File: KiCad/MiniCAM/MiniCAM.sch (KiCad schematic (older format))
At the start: 69 parts, among them J1 SMA-J-P-H-RA-TH1, J2 Conn_01x02, J3 Conn_01x03, J4 Conn_02x03_Odd_Even, U1 NCV8154MW180280TBG, U2 DS90UB933-Q1, U3 MT9P031, U4 SiT_2.5mmx2mm

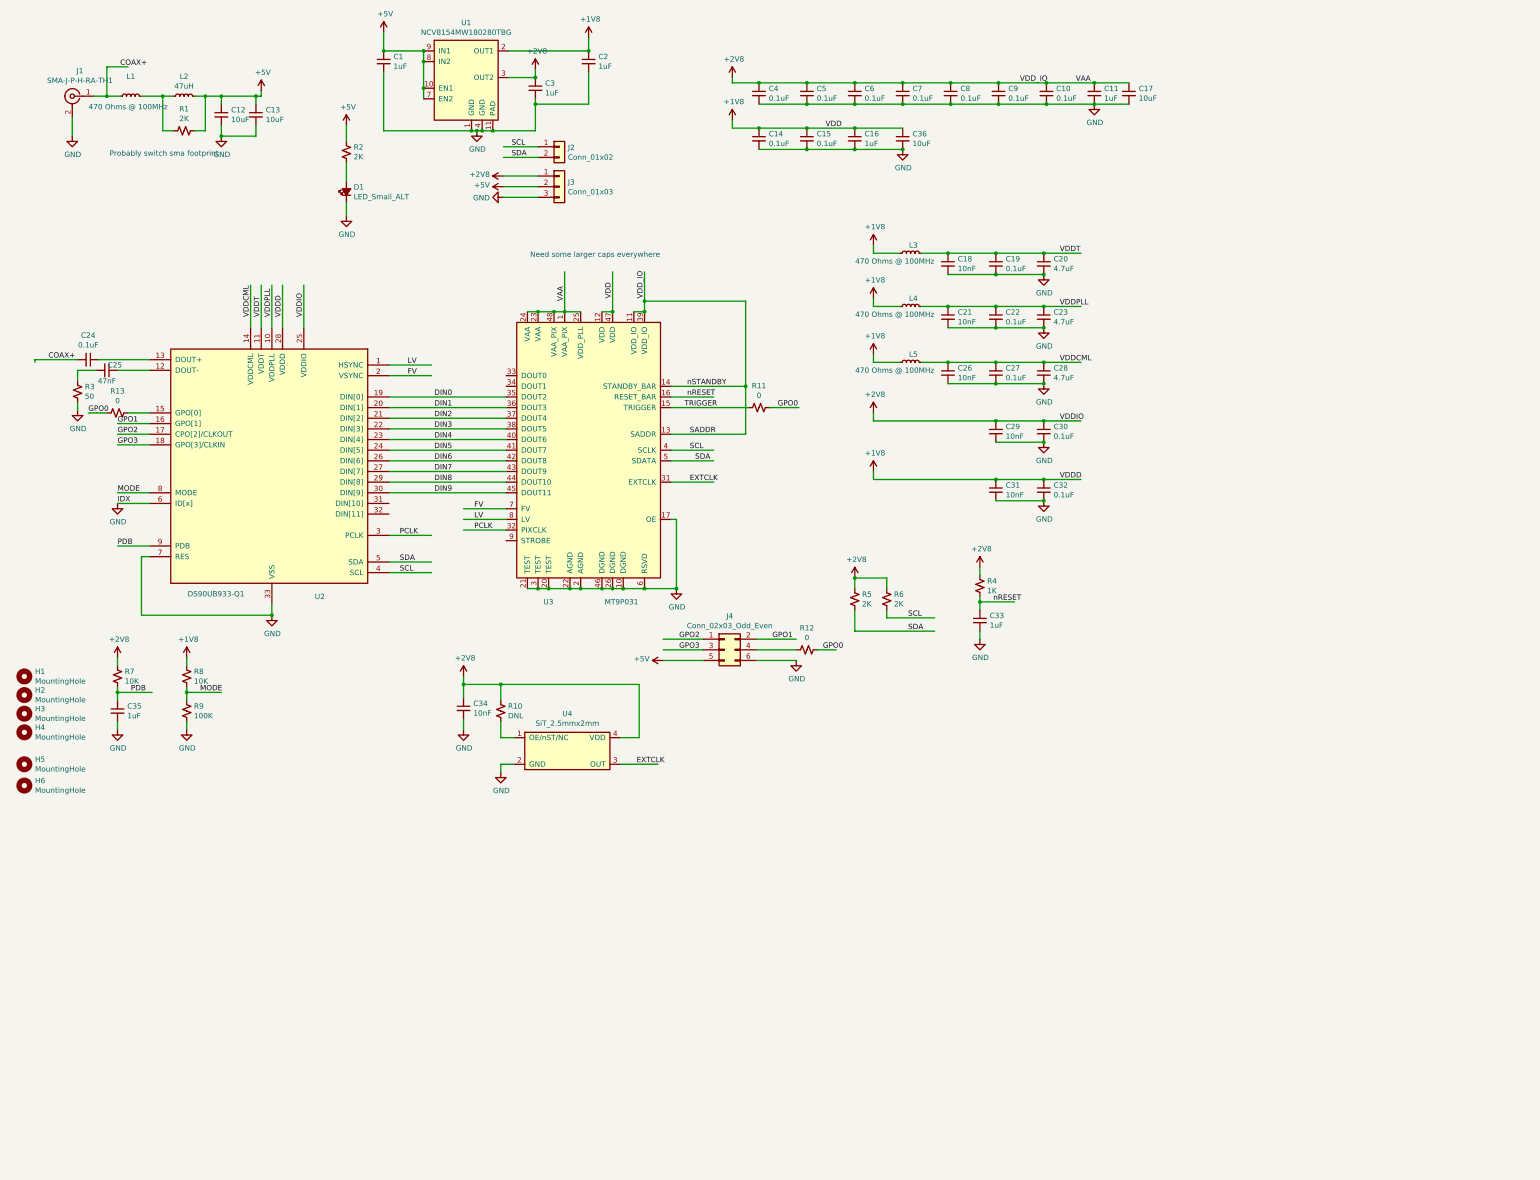
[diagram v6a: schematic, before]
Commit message: Clean up MiniCAM KiCad schematic
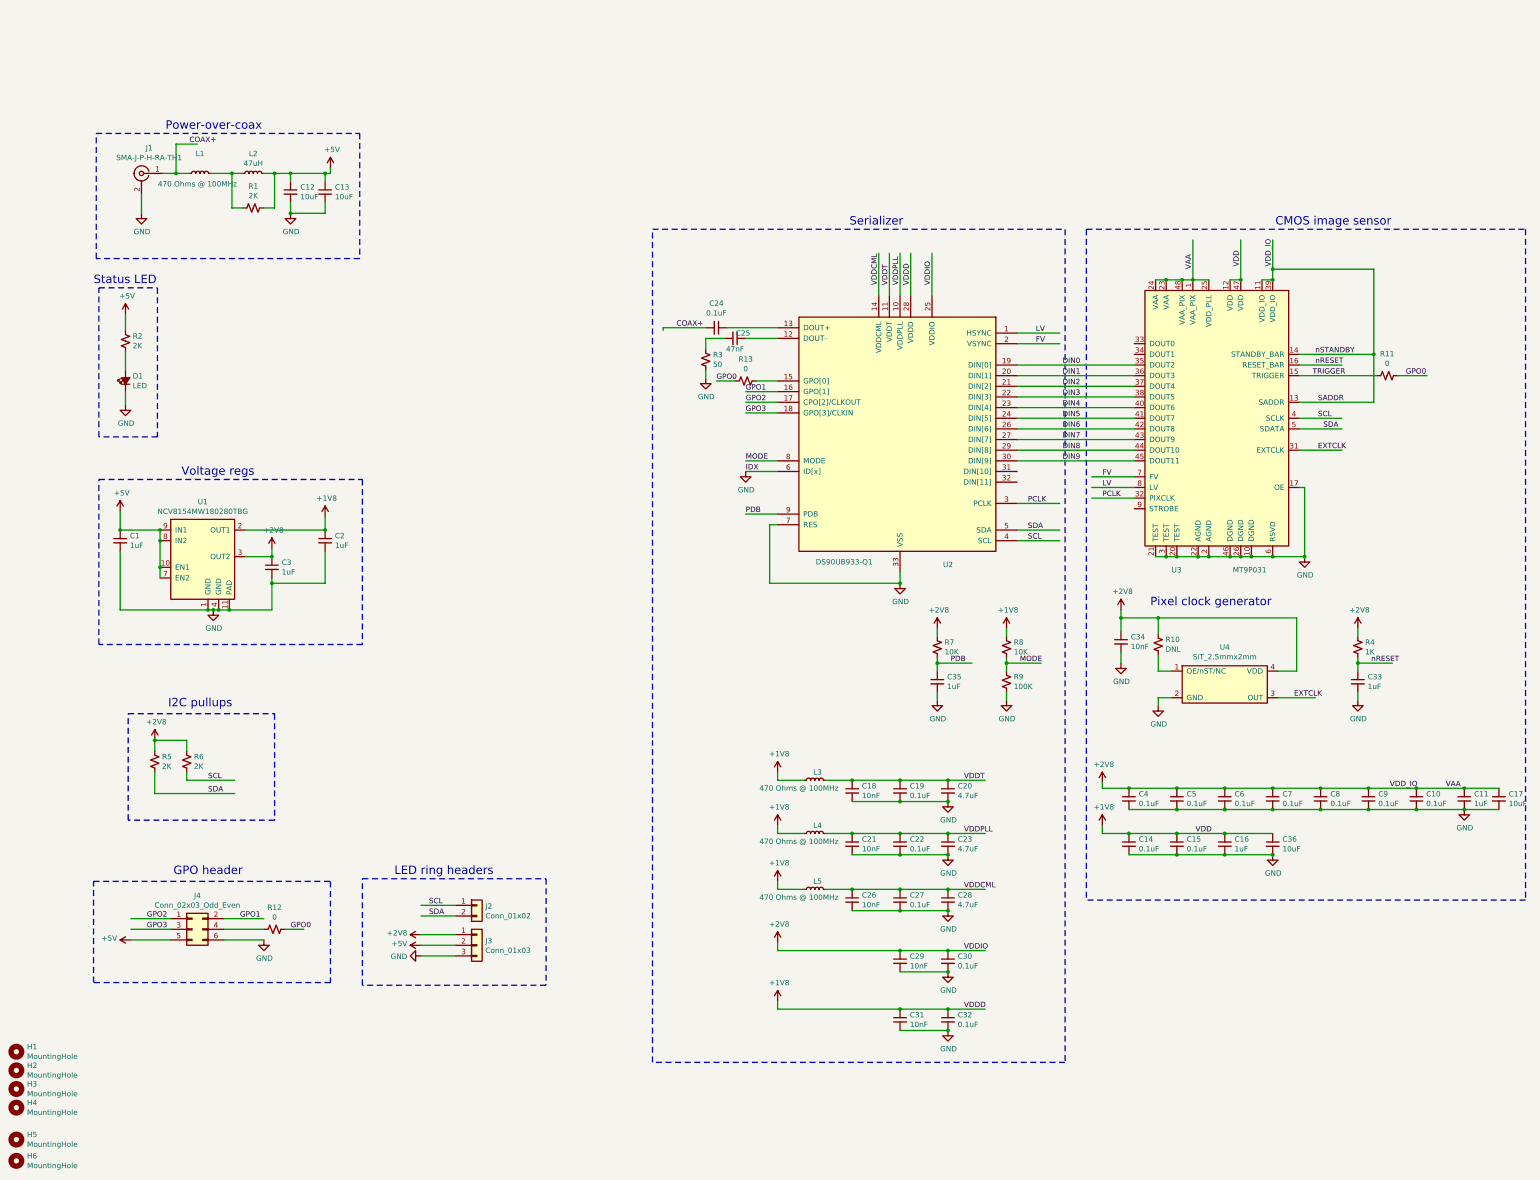
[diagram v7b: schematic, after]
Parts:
- D1: value LED_Small_ALT -> LED
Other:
- note added: "CMOS image sensor"
- note added: "GPO header"
- note added: "I2C pullups"
- note added: "LED ring headers"
- note added: "Pixel clock generator"
- note added: "Power-over-coax"
- note added: "Serializer"
- note added: "Status LED"
- note added: "Voltage regs"
- note removed: "Need some larger caps everywhere"
- note removed: "Probably switch sma footprint"
- moved on the sheet: C1, C10, C11, C12, C13, C14, C15, C16, C17, C18, C19, C2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
